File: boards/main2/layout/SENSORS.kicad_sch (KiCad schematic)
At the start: 63 parts, among them IC2 LSM6DSVTR, Q2 AO3400A, Q3 AO3400A, Q4 AO3400A, Q5 AO3400A, Q9 AO3400A, U10 INA241A2IDGKR, U11 INA241A2IDGKR, U12 TLV9001IDBVR

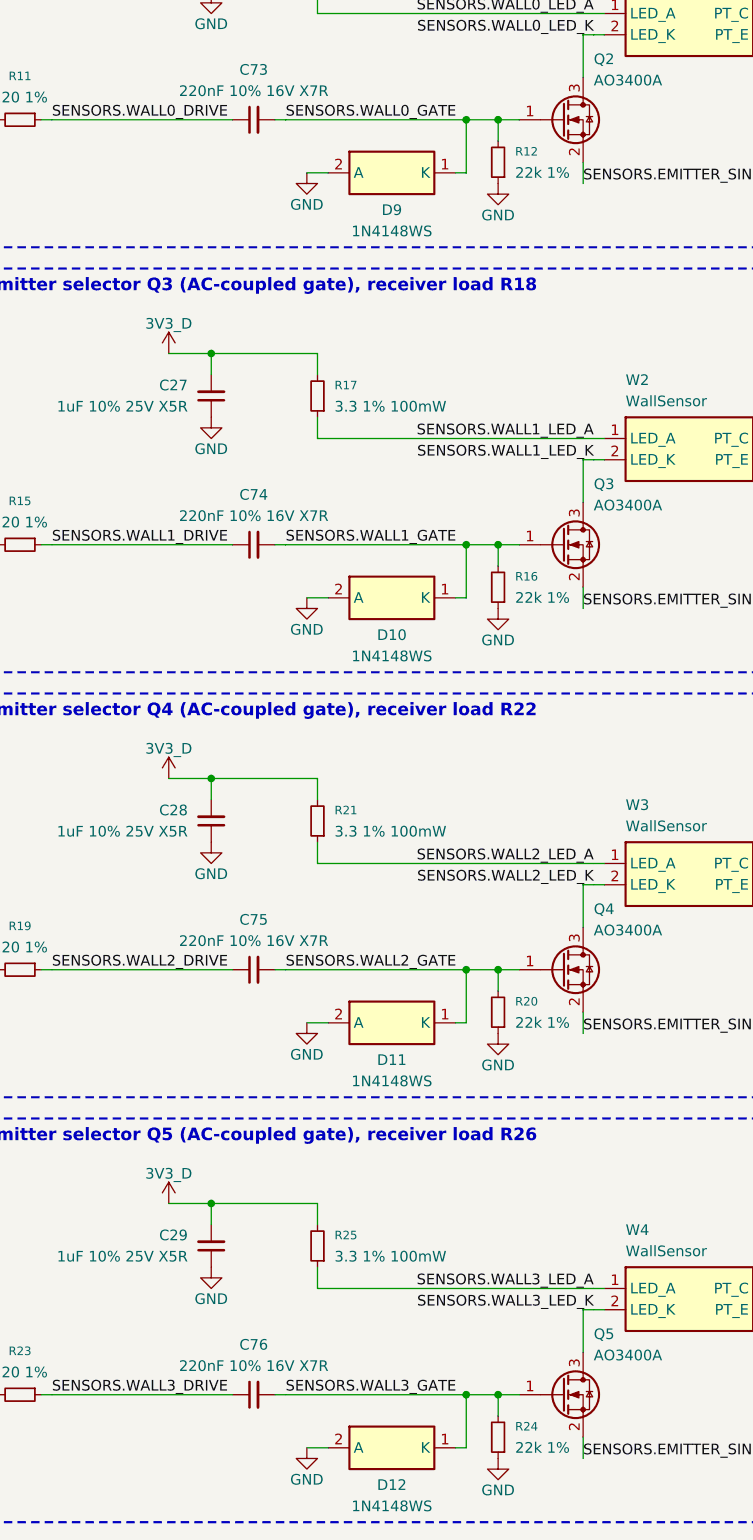
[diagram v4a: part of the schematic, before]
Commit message: 🎨 Draw the diodes and buzzer as symbols, and make D4 blue
- 1N4148WS, B5819W and FUET-5030: replace the box bodies with diode,
  Schottky and buzzer symbols (same pins). Nudge D3 and BZ1 on both boards'
  PERIPHERALS sheets.
- D4: KENTO KT-0603B blue (C2288, VF 2.6-3.1 V at 5 mA) instead of the
  yellow NCD0603Y2. R4 goes from 680 Ohm to 100 Ohm: 1.2 mA at the worst
  bin and rail, 7.5 mA at most. LED_YELLOW_A is renamed LED_BLUE_A.
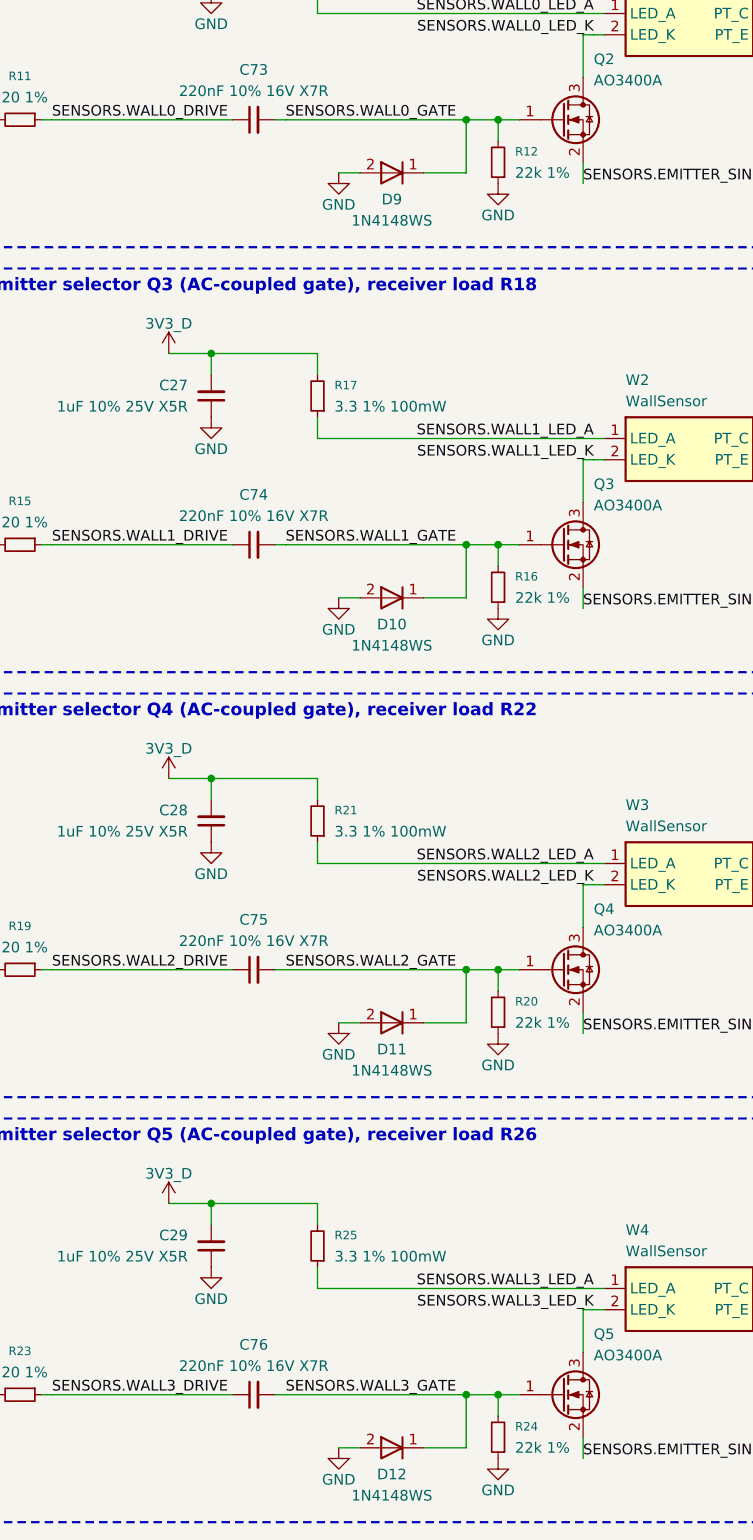
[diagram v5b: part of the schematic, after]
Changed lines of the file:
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@@
 		(dnp no)
 		(property "Reference" "D12"
-			(at 85.09 277.495 0)
+			(at 85.09 276.225 0)
 			(show_name no)
 			(do_not_autoplace no)
@@
 		)
 		(property "Value" "1N4148WS"
-			(at 85.09 280.035 0)
+			(at 85.09 278.765 0)
 			(show_name no)
 			(do_not_autoplace no)
@@
 		(dnp no)
 		(property "Reference" "D11"
-			(at 85.09 226.695 0)
+			(at 85.09 225.425 0)
 			(show_name no)
 			(do_not_autoplace no)
@@
 		)
 		(property "Value" "1N4148WS"
-			(at 85.09 229.235 0)
+			(at 85.09 227.965 0)
 			(show_name no)
 			(do_not_autoplace no)
@@
 		(dnp no)
 		(property "Reference" "D9"
-			(at 85.09 125.095 0)
+			(at 85.09 123.825 0)
 			(show_name no)
 			(do_not_autoplace no)
@@
 		)
 		(property "Value" "1N4148WS"
-			(at 85.09 127.635 0)
+			(at 85.09 126.365 0)
 			(show_name no)
 			(do_not_autoplace no)
@@
 		(dnp no)
 		(property "Reference" "D10"
-			(at 85.09 175.895 0)
+			(at 85.09 174.625 0)
 			(show_name no)
 			(do_not_autoplace no)
@@
 		)
 		(property "Value" "1N4148WS"
-			(at 85.09 178.435 0)
+			(at 85.09 177.165 0)
 			(show_name no)
 			(do_not_autoplace no)
@@
 	(wire
 		(pts
-			(xy 92.71 120.65) (xy 93.98 120.65)
+			(xy 88.9 120.65) (xy 93.98 120.65)
 		)
 		(stroke
@@
 	(wire
 		(pts
-			(xy 92.71 171.45) (xy 93.98 171.45)
+			(xy 88.9 171.45) (xy 93.98 171.45)
 		)
 		(stroke
@@
 	(wire
 		(pts
-			(xy 92.71 222.25) (xy 93.98 222.25)
+			(xy 88.9 222.25) (xy 93.98 222.25)
 		)
 		(stroke
@@
 	(wire
 		(pts
-			(xy 92.71 273.05) (xy 93.98 273.05)
+			(xy 88.9 273.05) (xy 93.98 273.05)
 		)
 		(stroke
@@
 	(wire
 		(pts
-			(xy 77.47 171.45) (xy 74.93 171.45)
+			(xy 81.28 171.45) (xy 78.74 171.45)
 		)
 		(stroke
@@
 	(wire
 		(pts
-			(xy 77.47 222.25) (xy 74.93 222.25)
+			(xy 81.28 222.25) (xy 78.74 222.25)
 		)
 		(stroke
@@
 	(wire
 		(pts
-			(xy 77.47 273.05) (xy 74.93 273.05)
+			(xy 81.28 273.05) (xy 78.74 273.05)
 		)
 		(stroke
@@
 	(wire
 		(pts
-			(xy 77.47 120.65) (xy 74.93 120.65)
+			(xy 81.28 120.65) (xy 78.74 120.65)
 		)
 		(stroke
@@
 	(symbol
 		(lib_id "GND")
-		(at 74.93 171.45 0)
+		(at 78.74 171.45 0)
 		(unit 1)
 		(body_style 1)
@@
 		(dnp no)
 		(property "Reference" "#PWRd469141afd395ca796e8243d3a0729f3"
-			(at 74.93 171.45 0)
+			(at 78.74 171.45 0)
 			(hide yes)
 			(show_name no)
@@
 		)
 		(property "Value" "GND"
-			(at 74.93 175.26 0)
+			(at 78.74 175.26 0)
 			(show_name no)
 			(do_not_autoplace no)
@@
 		)
 		(property "Footprint" ""
-			(at 74.93 171.45 0)
+			(at 78.74 171.45 0)
 			(hide yes)
 			(show_name no)
@@
 		)
 		(property "Datasheet" ""
-			(at 74.93 171.45 0)
+			(at 78.74 171.45 0)
 			(hide yes)
 			(show_name no)
@@
 		)
 		(property "Description" "Power symbol creates a global label with name \"GND\" , ground"
-			(at 74.93 171.45 0)
+			(at 78.74 171.45 0)
 			(hide yes)
 			(show_name no)
@@
 		)
 		(property "ki_keywords" "global power"
-			(at 74.93 171.45 0)
+			(at 78.74 171.45 0)
 			(hide yes)
 			(show_name no)
@@
 	(symbol
 		(lib_id "GND")
-		(at 74.93 222.25 0)
+		(at 78.74 222.25 0)
 		(unit 1)
 		(body_style 1)
@@
 		(dnp no)
 		(property "Reference" "#PWR929fc5e557125cab995b918760b992c1"
-			(at 74.93 222.25 0)
+			(at 78.74 222.25 0)
 			(hide yes)
 			(show_name no)
@@
 		)
 		(property "Value" "GND"
-			(at 74.93 226.06 0)
+			(at 78.74 226.06 0)
 			(show_name no)
 			(do_not_autoplace no)
@@
 		)
 		(property "Footprint" ""
-			(at 74.93 222.25 0)
+			(at 78.74 222.25 0)
 			(hide yes)
 			(show_name no)
@@
 		)
 		(property "Datasheet" ""
-			(at 74.93 222.25 0)
+			(at 78.74 222.25 0)
 			(hide yes)
 			(show_name no)
@@
 		)
 		(property "Description" "Power symbol creates a global label with name \"GND\" , ground"
-			(at 74.93 222.25 0)
+			(at 78.74 222.25 0)
 			(hide yes)
 			(show_name no)
@@
 		)
 		(property "ki_keywords" "global power"
-			(at 74.93 222.25 0)
+			(at 78.74 222.25 0)
 			(hide yes)
 			(show_name no)
@@
 	(symbol
 		(lib_id "GND")
-		(at 74.93 273.05 0)
+		(at 78.74 273.05 0)
 		(unit 1)
 		(body_style 1)
@@
 		(dnp no)
 		(property "Reference" "#PWRd9b7cd9dcb4a53bf8315cf7027f37f72"
-			(at 74.93 273.05 0)
+			(at 78.74 273.05 0)
 			(hide yes)
 			(show_name no)
@@
 		)
 		(property "Value" "GND"
-			(at 74.93 276.86 0)
+			(at 78.74 276.86 0)
 			(show_name no)
 			(do_not_autoplace no)
@@
 		)
 		(property "Footprint" ""
-			(at 74.93 273.05 0)
+			(at 78.74 273.05 0)
 			(hide yes)
 			(show_name no)
@@
 		)
 		(property "Datasheet" ""
-			(at 74.93 273.05 0)
+			(at 78.74 273.05 0)
 			(hide yes)
 			(show_name no)
@@
 		)
 		(property "Description" "Power symbol creates a global label with name \"GND\" , ground"
-			(at 74.93 273.05 0)
+			(at 78.74 273.05 0)
 			(hide yes)
 			(show_name no)
@@
 		)
 		(property "ki_keywords" "global power"
-			(at 74.93 273.05 0)
+			(at 78.74 273.05 0)
 			(hide yes)
 			(show_name no)
@@
 	(symbol
 		(lib_id "GND")
-		(at 74.93 120.65 0)
+		(at 78.74 120.65 0)
 		(unit 1)
 		(body_style 1)
@@
 		(dnp no)
 		(property "Reference" "#PWRf67b1ab725165396abda0d72df56e2a0"
-			(at 74.93 120.65 0)
+			(at 78.74 120.65 0)
 			(hide yes)
 			(show_name no)
@@
 		)
 		(property "Value" "GND"
-			(at 74.93 124.46 0)
+			(at 78.74 124.46 0)
 			(show_name no)
 			(do_not_autoplace no)
@@
 		)
 		(property "Footprint" ""
-			(at 74.93 120.65 0)
+			(at 78.74 120.65 0)
 			(hide yes)
 			(show_name no)
@@
 		)
 		(property "Datasheet" ""
-			(at 74.93 120.65 0)
+			(at 78.74 120.65 0)
 			(hide yes)
 			(show_name no)
@@
 		)
 		(property "Description" "Power symbol creates a global label with name \"GND\" , ground"
-			(at 74.93 120.65 0)
+			(at 78.74 120.65 0)
 			(hide yes)
 			(show_name no)
@@
 		)
 		(property "ki_keywords" "global power"
-			(at 74.93 120.65 0)
+			(at 78.74 120.65 0)
 			(hide yes)
 			(show_name no)

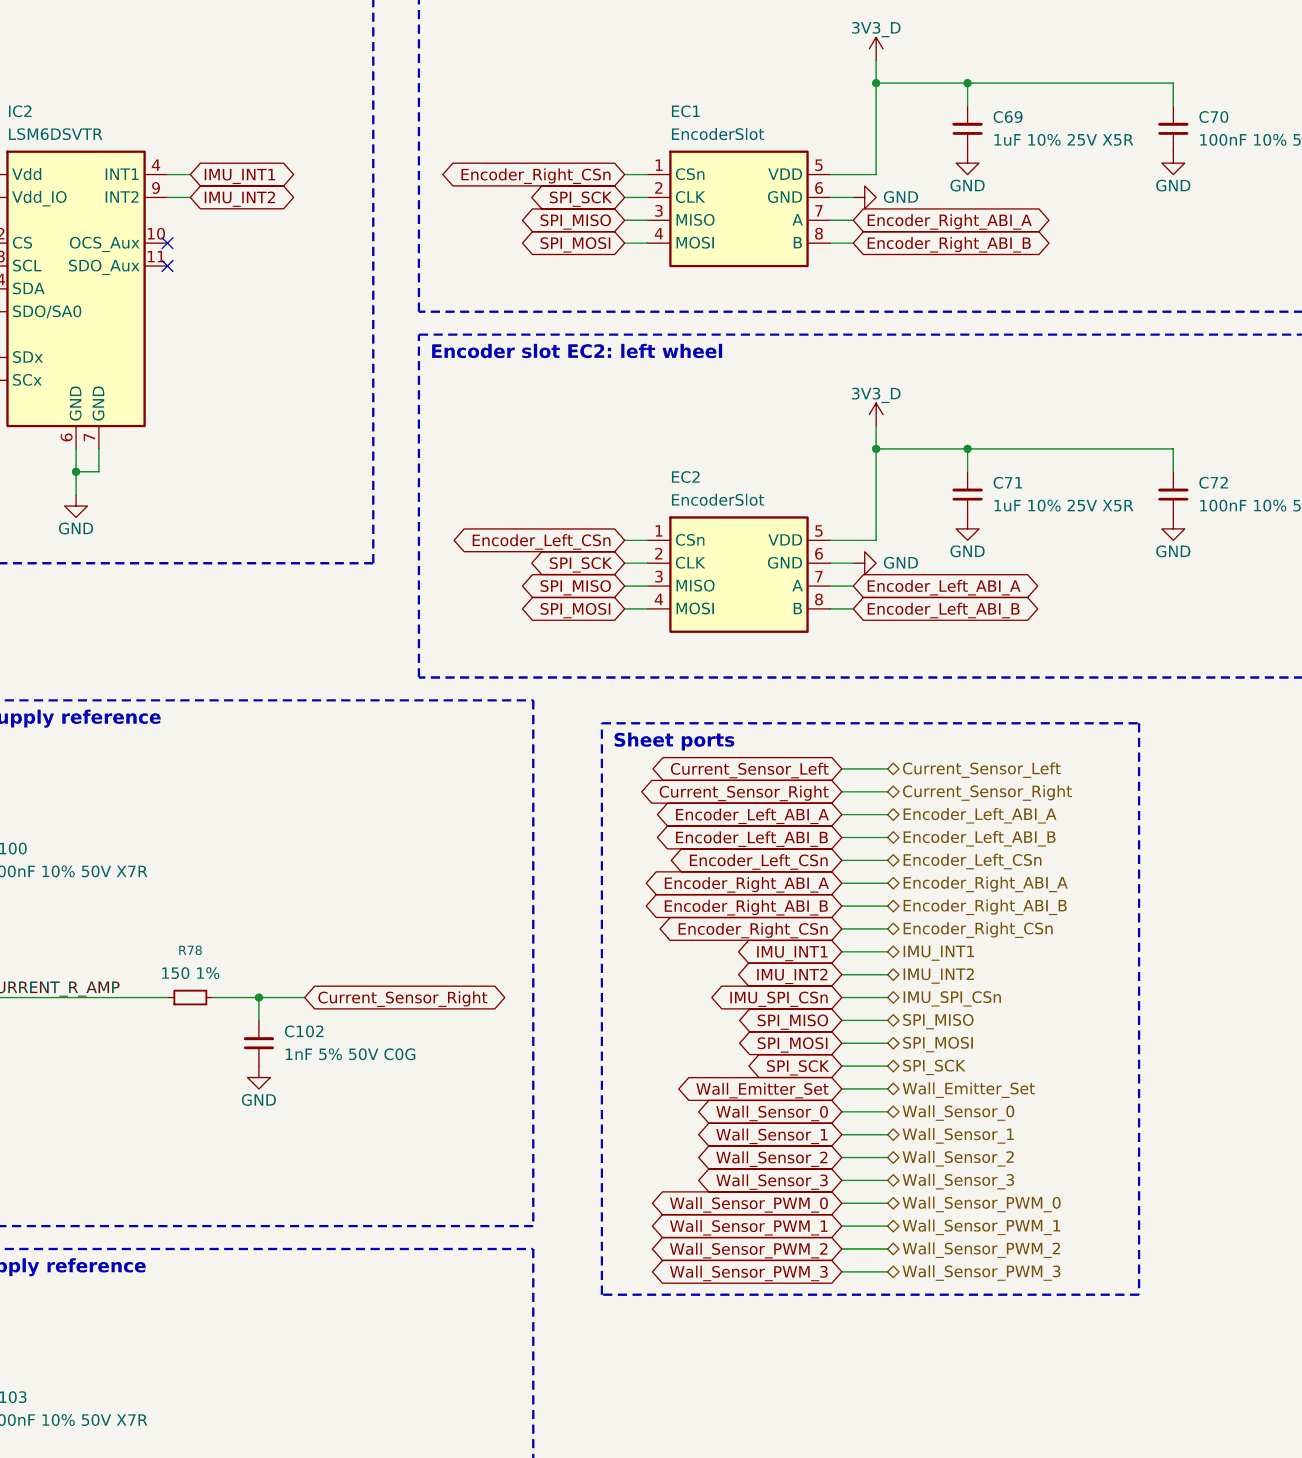
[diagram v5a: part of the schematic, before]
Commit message: 🚧 Swap main2's USB and ESP32-S3 for an ESP32-C5 and programming headers
Schematic and component checkpoint; the layout follows in its own commit.

- Remove USB-C, its ESD, power path and VBUS sense; both MCUs flash over
  the air.
- U13 ESP32-C5-MINI-1-N4 (dual-band, 5 GHz channels 36-48) in the
  rear-right corner, with its antenna notch on the right edge. SW4 and its
  notch move to the rear-left.
- H7-C5 link: SPI2 half-duplex 3-wire (PA12 SCK, PA11 CSn, PB14 DATA with
  IOSWP), PA9 flow control, UART4 fallback on the same pins. Fan_Enable
  moves to PB10, IMU INT1 to PB6, INT2 is left open.
- J2: 2x3 1.27 mm header in the ESP-Prog layout. SWD1: 1x4 1.27 mm in
  clone ST-Link order (SWDIO, GND, SWCLK, 5V). 5V_IN feeds VSYS through
  D17 (B5819W) to flash without the battery.
- R44/R45 to 20k/2k keeps PC5 below its absolute maximum at the clamp.
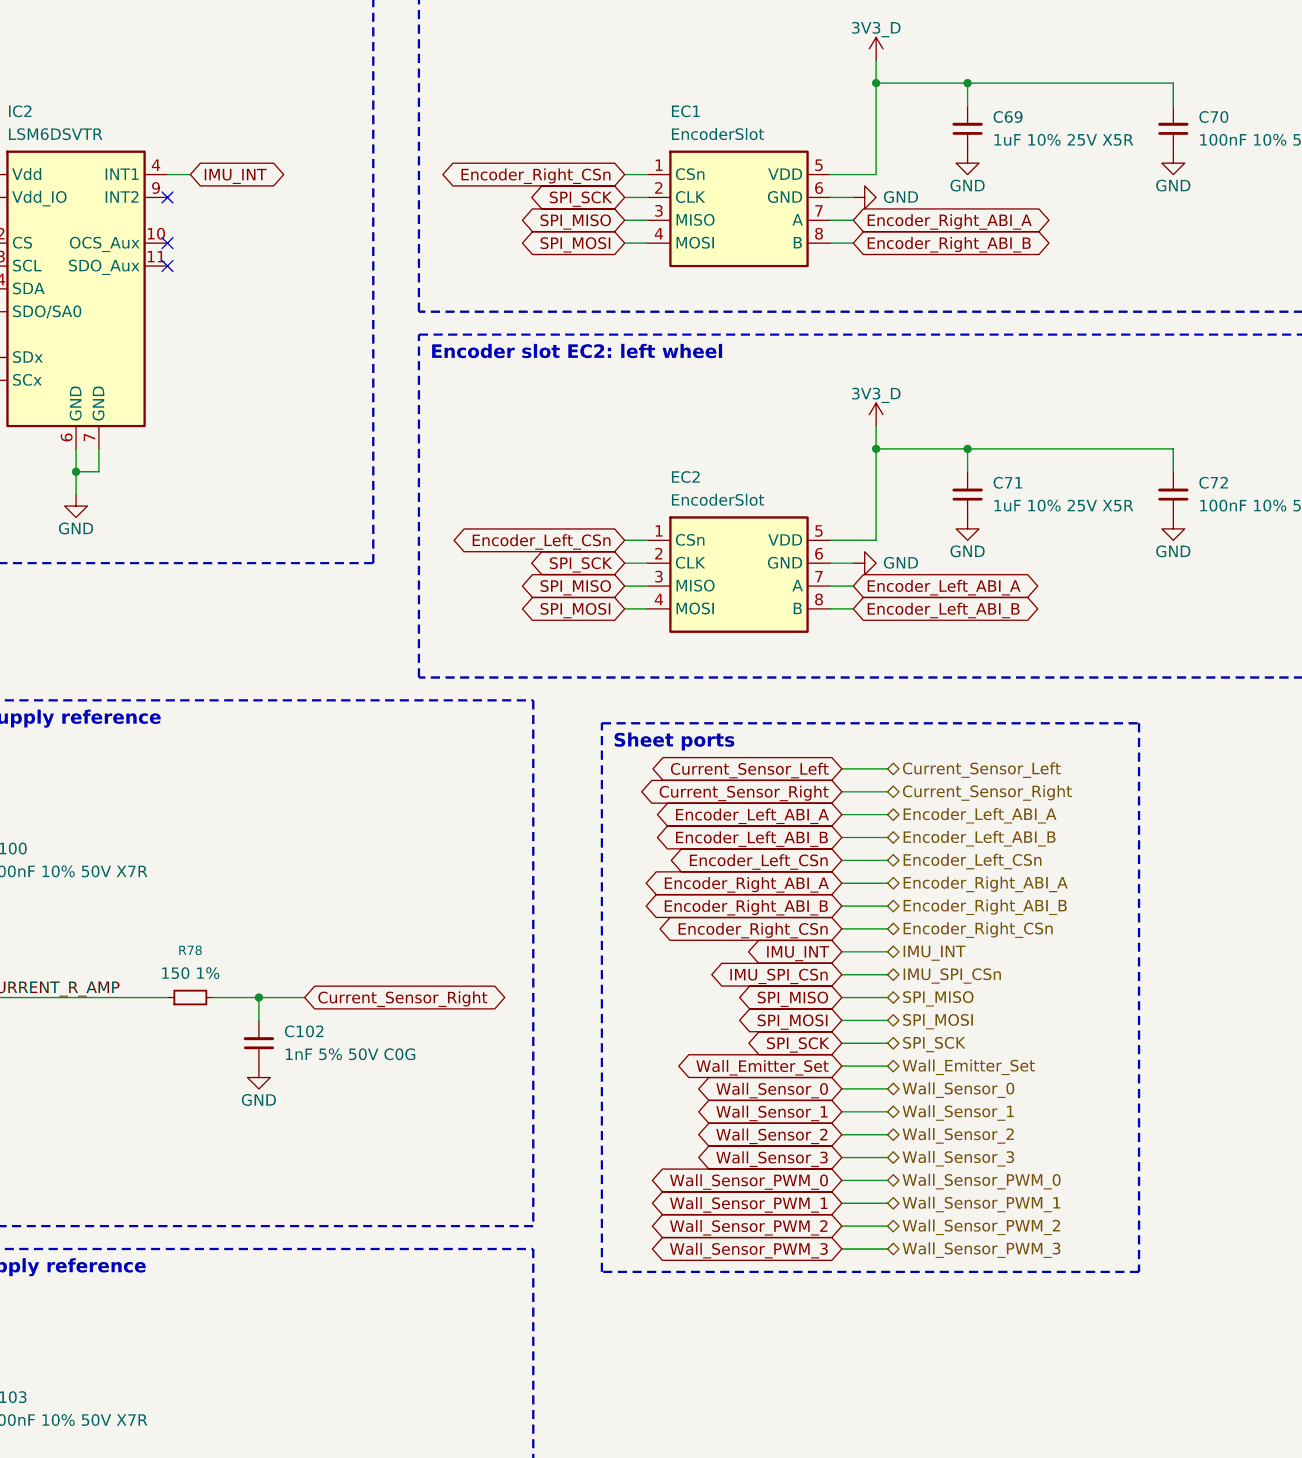
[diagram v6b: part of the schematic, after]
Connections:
- net IMU_INT1 renamed IMU_INT
- net IMU_INT2: no longer names the net of IC2.9 (INT2)
- no-connect marks 2 -> 3
